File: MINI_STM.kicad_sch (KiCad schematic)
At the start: 4 parts, among them U1 STM32G431KBTx, U2 LD1117S50TR_SOT223

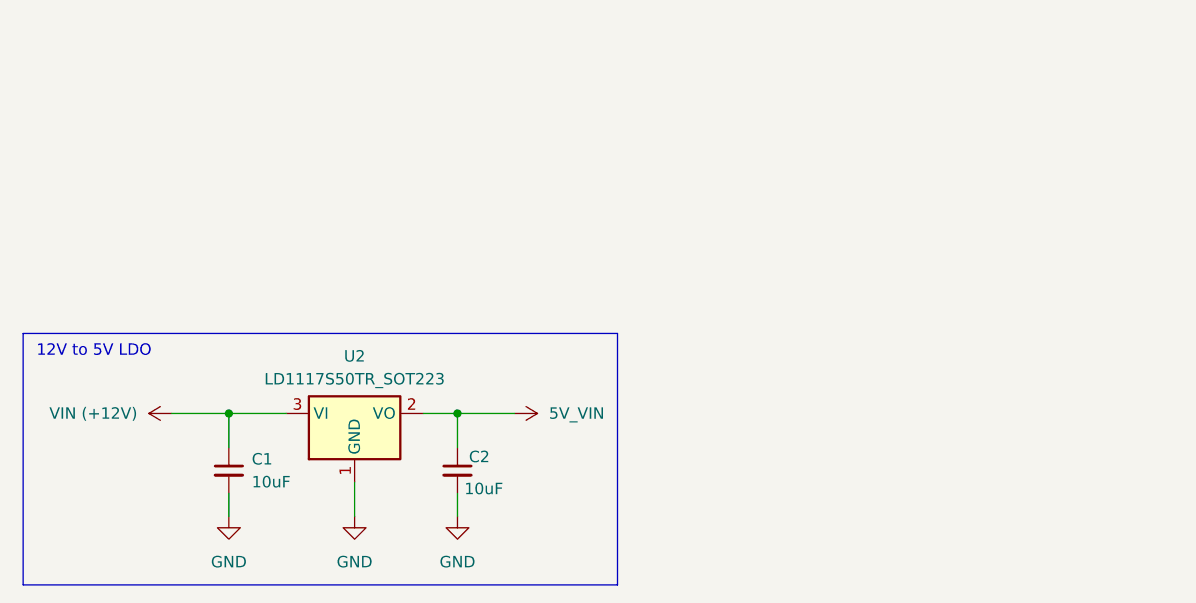
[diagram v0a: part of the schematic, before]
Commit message: Changed LDO to buck regulator.
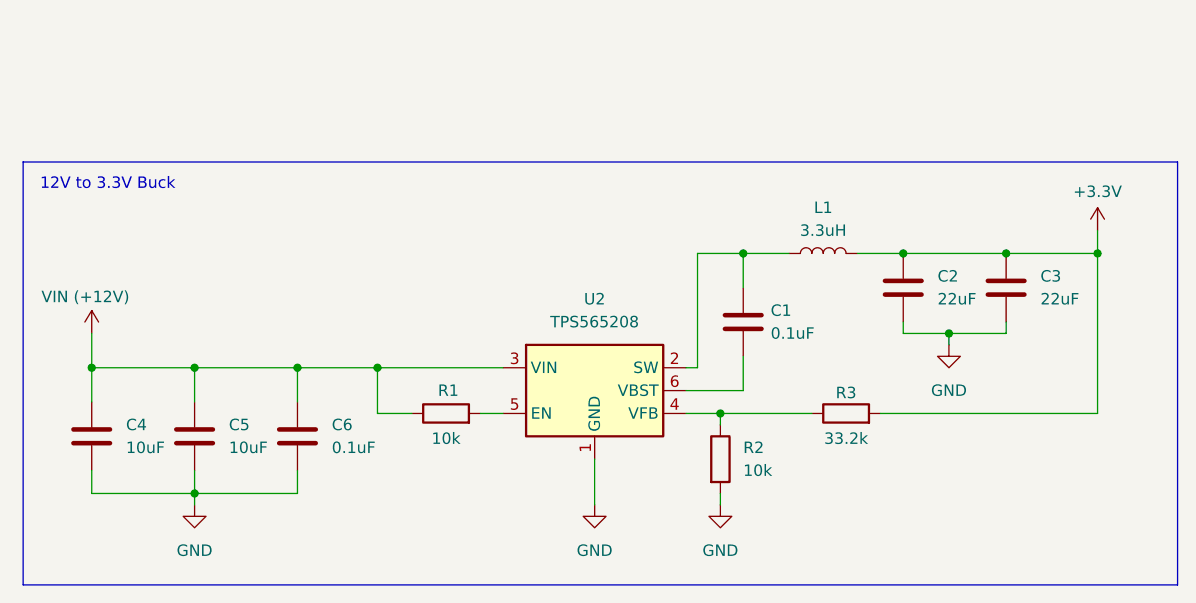
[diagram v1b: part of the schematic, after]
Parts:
- removed C1, C2: 10uF, symbol Device:C_Small
- removed U2: LD1117S50TR_SOT223, Package_TO_SOT_SMD:SOT-223-3_TabPin2, symbol Regulator_Linear:LD1117S50TR_SOT223
- added C1, C6: 0.1uF, symbol Device:C
- added C2, C3: 22uF, symbol Device:C
- added C4, C5: 10uF, symbol Device:C
- added L1: 3.3uH, symbol Device:L
- added R1, R2: 10k, symbol Device:R
- added R3: 33.2k, symbol Device:R
- added U2: TPS565208, Package_TO_SOT_SMD:SOT-23-6, symbol Regulator_Switching:TPS565208
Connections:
- net GND: now also C2.2, C3.2, C4.2, C5.2, C6.2, R2.2, U2.1 (GND)
- net VIN (+12V): now also C4.1, C5.1, C6.1, R1.1, U2.3 (VIN)
- new net: R1.2, U2.5 (EN)
- new net: R2.1, R3.1, U2.4 (VFB)
- new net: C1.2, L1.1, U2.2 (SW)
- new net: C1.1, U2.6 (VBST)
- new net +3.3V: C2.1, C3.1, L1.2, R3.2
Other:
- note added: "12V to 3.3V Buck"
- note removed: "12V to 5V LDO"

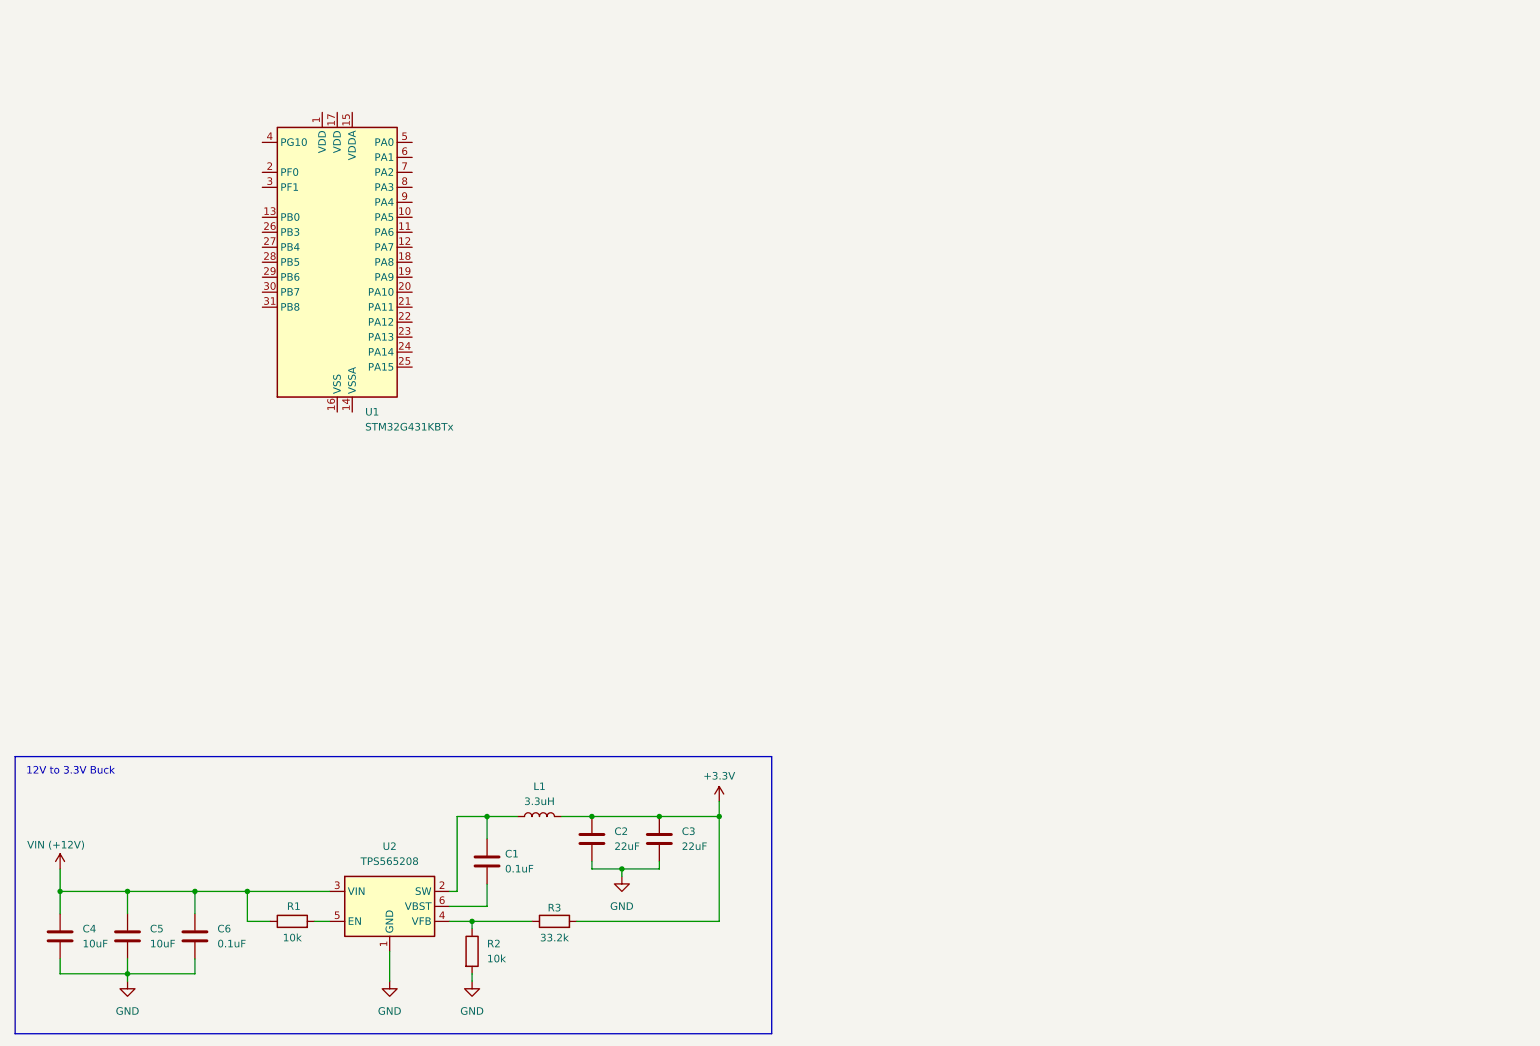
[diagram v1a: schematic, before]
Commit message: NRST circuitry added.
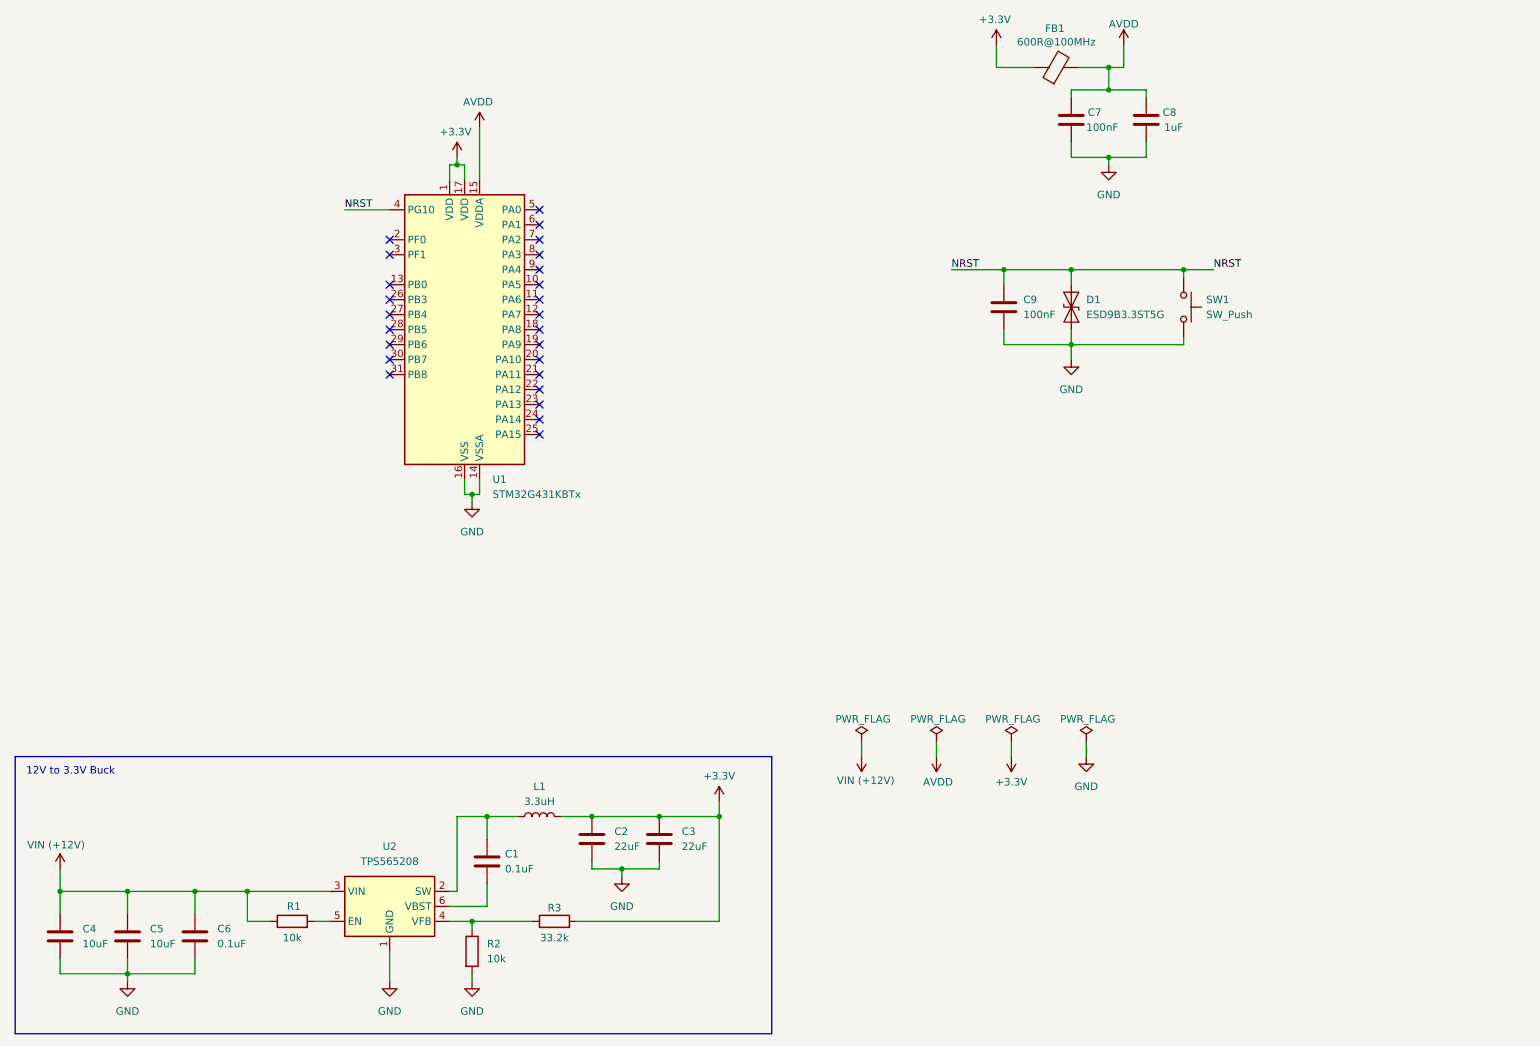
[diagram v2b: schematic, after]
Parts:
- added C7, C9: 100nF, symbol Device:C
- added C8: 1uF, symbol Device:C
- added D1: ESD9B3.3ST5G, Diode_SMD:D_SOD-923, symbol Diode:ESD9B3.3ST5G
- added FB1: 600R@100MHz, symbol Device:FerriteBead
- added SW1: SW_Push, symbol Switch:SW_Push
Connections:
- net +3.3V: now also U1.1 (VDD), U1.17 (VDD), FB1.1
- net GND: now also U1.14 (VSSA), U1.16 (VSS), U1.32 (VSS), C7.2, C8.2, C9.2, D1.1 (A1), SW1.2
- net AVDD: now reaches U1.15 (VDDA)
- net AVDD: now also C7.1, C8.1, FB1.2
- net NRST: now reaches U1.4 (PG10)
- net NRST: now also C9.1, D1.2 (A2), SW1.1
- no-connect marks 0 -> 25
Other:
- moved on the sheet: U1

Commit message: Cleaned up schematic and added programming connector.
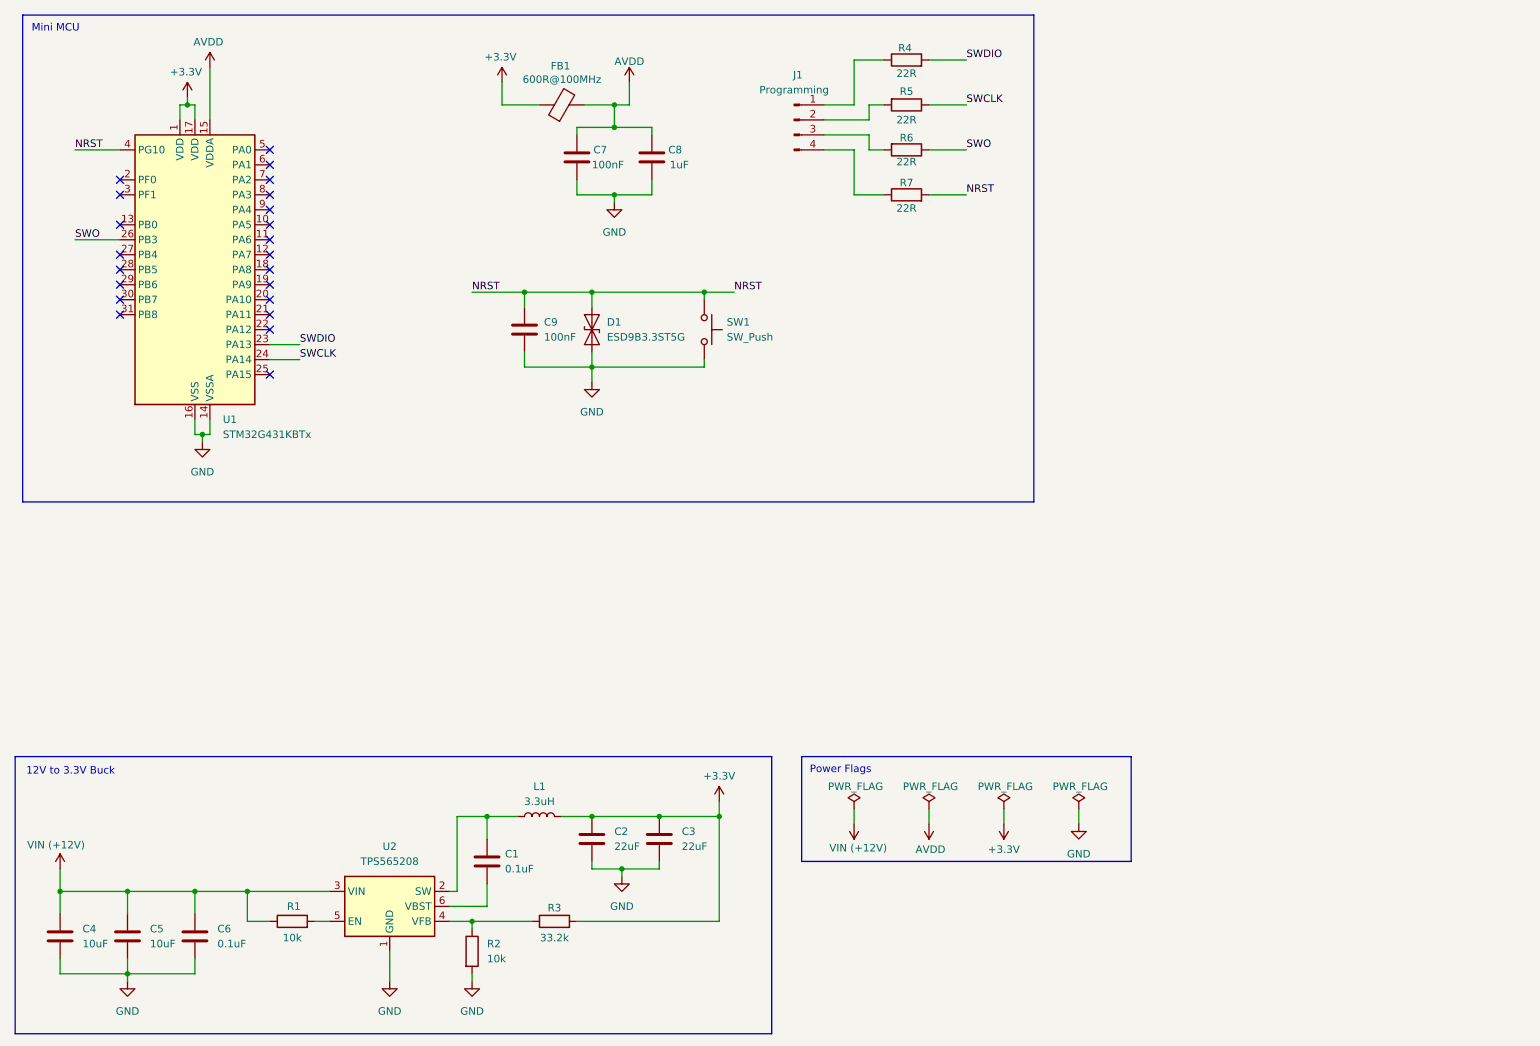
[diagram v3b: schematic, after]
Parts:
- added J1: Programming, symbol Connector:Conn_01x04_Pin
- added R4, R5, R6, R7: 22R, symbol Device:R
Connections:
- net NRST: now also R7.2
- net SWDIO: now reaches U1.23 (PA13)
- net SWDIO: now also R4.2
- net SWCLK: now reaches U1.24 (PA14)
- net SWCLK: now also R5.1
- net SWO: now reaches U1.26 (PB3)
- net SWO: now also R6.1
- new net: J1.1 (Pin_1), R4.1
- new net: J1.2 (Pin_2), R5.2
- new net: J1.3 (Pin_3), R6.2
- new net: J1.4 (Pin_4), R7.1
- no-connect marks 25 -> 22
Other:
- note added: "Mini MCU"
- note added: "Power Flags"
- moved on the sheet: C7, C8, C9, D1, FB1, SW1, U1

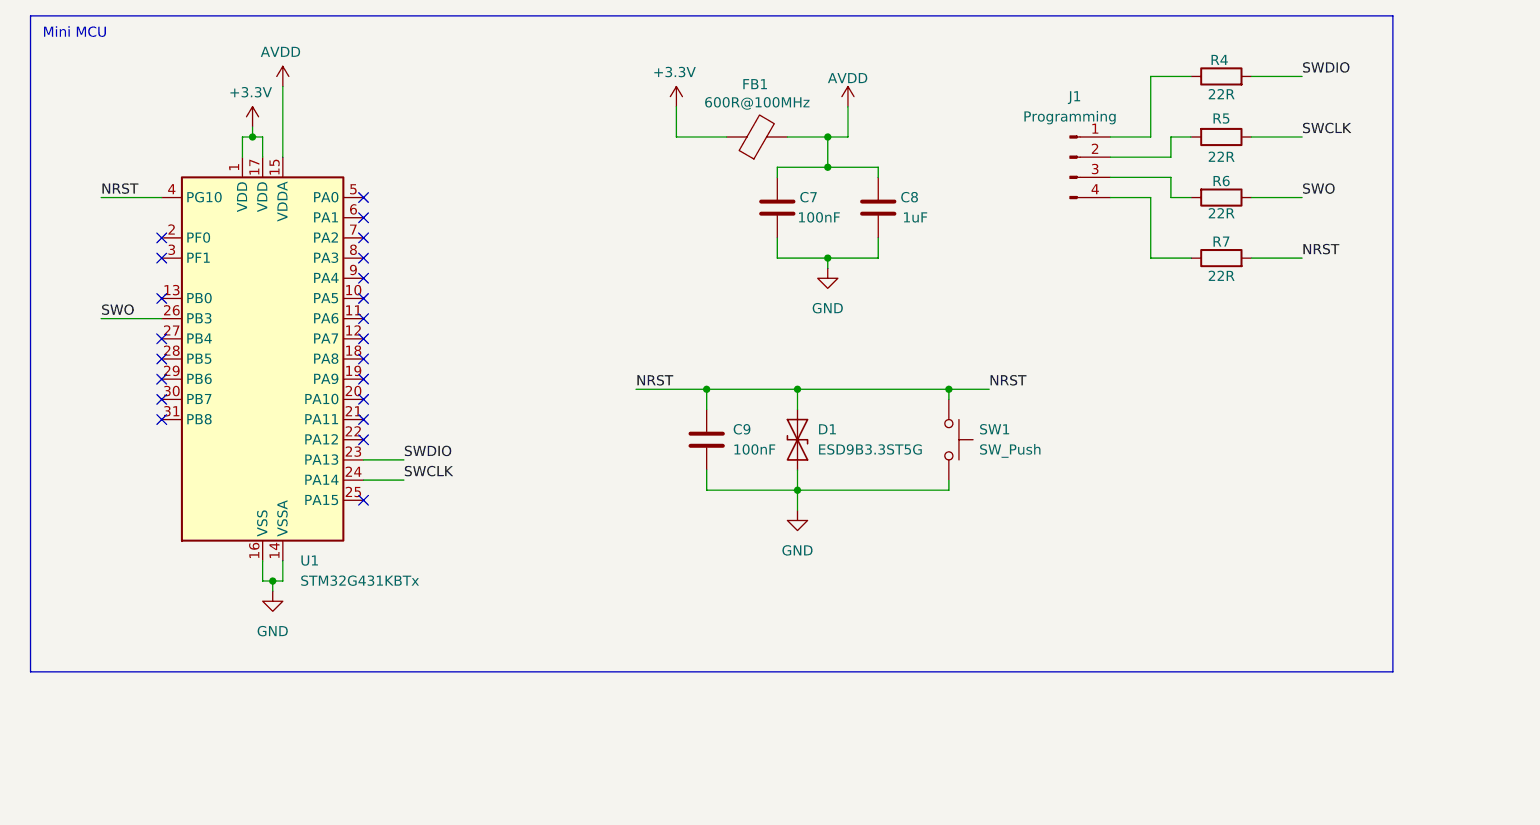
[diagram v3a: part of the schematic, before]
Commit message: Updates to prgramming connection.
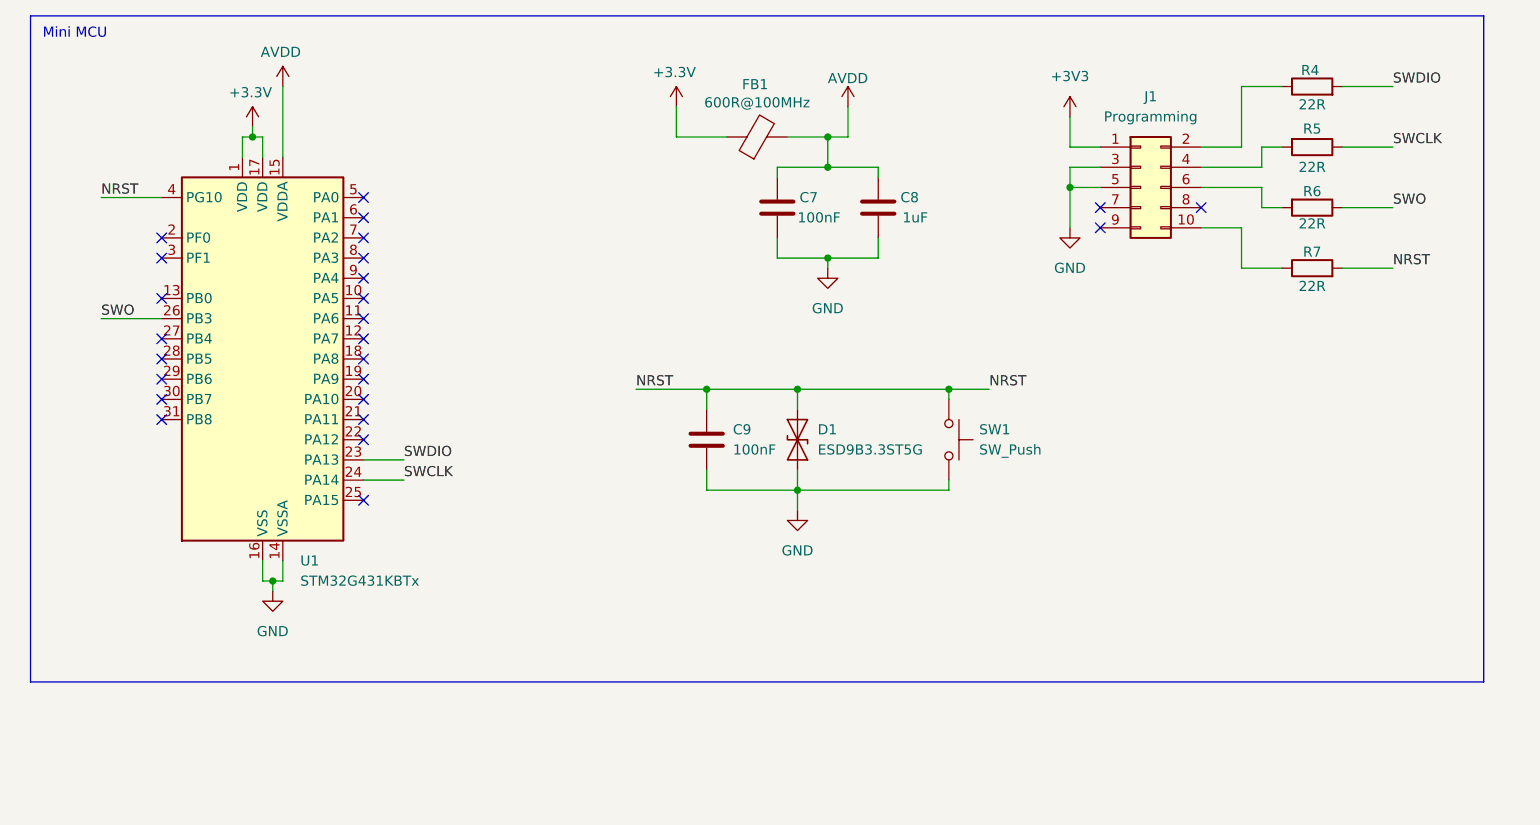
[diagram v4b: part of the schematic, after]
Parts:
- removed J1: Programming, symbol Connector:Conn_01x04_Pin
- added J1: Programming, symbol Connector_Generic:Conn_02x05_Odd_Even
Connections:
- net GND: now also J1.3 (Pin_3), J1.5 (Pin_5)
- net at R4.1: now also J1.2 (Pin_2)
- net at R5.2: now also J1.4 (Pin_4)
- net at R6.2: now also J1.6 (Pin_6)
- net at R7.1: now also J1.10 (Pin_10)
- new net +3V3: J1.1 (Pin_1)
- no-connect marks 22 -> 25
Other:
- moved on the sheet: R4, R5, R6, R7

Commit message: Added oscillator circuit, but it is not necessary.
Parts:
- added C10, C11: 14pF, symbol Device:C
- added JP1: OSC_IN JP, symbol Jumper:SolderJumper_2_Bridged
- added JP2: OSC_OUT JP, symbol Jumper:SolderJumper_2_Bridged
- added X1: ~, symbol Oscillator:ATS240C-E
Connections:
- net +3.3V is gone; now on net +3V3: C2.1, C3.1, FB1.1, L1.2, R3.2, U1.1 (VDD), U1.17 (VDD)
- net GND: now also C10.1, C11.1, X1.2 (GND), X1.4 (GND)
- net at U1.2 (PF0): now also JP1.2 (B)
- net at U1.3 (PF1): now also JP2.2 (B)
- new net OSC_IN: C10.2, JP1.1 (A), X1.1
- new net OSC_OUT: C11.2, JP2.1 (A), X1.3
- no-connect marks 25 -> 23
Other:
- moved on the sheet: C7, C8, C9, D1, FB1, SW1, U1

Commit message: Added more decoupling capacitors and power LED.
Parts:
- added C12, C13: 100nF, symbol Device:C
- added C14: 4.7uF, symbol Device:C
- added D2: Green, symbol Device:LED
- added R8: 150R, symbol Device:R
- C7: value 100nF -> 10nF
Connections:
- net +3V3: now also C12.1, C13.1, C14.1, R8.1
- net GND: now also C12.2, C13.2, C14.2, D2.1 (K)
- new net: D2.2 (A), R8.2
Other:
- note added: "Power LED"
- moved on the sheet: C10, C11, C7, C8, C9, D1, FB1, J1, JP1, JP2, R4, R5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
